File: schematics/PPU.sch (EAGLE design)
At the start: 51 parts, among them Q1 KN2222A, Q2 KIA431, Q3 2SC945, U12 UM6618, U13 53.693175MHz, U3 UM70C188, U4 KA2195D, U5 UM611024, U6 UM611024

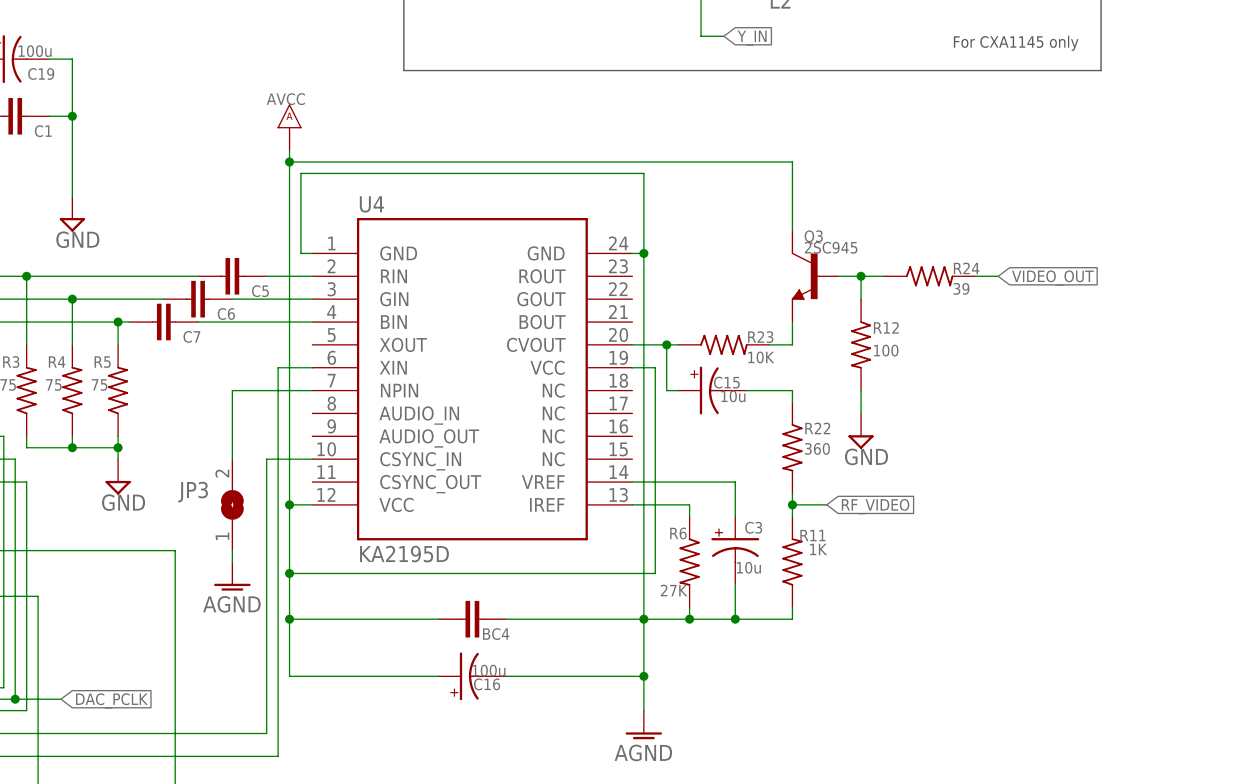
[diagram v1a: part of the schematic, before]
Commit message: Correct Q3 related wiring
(CV output)
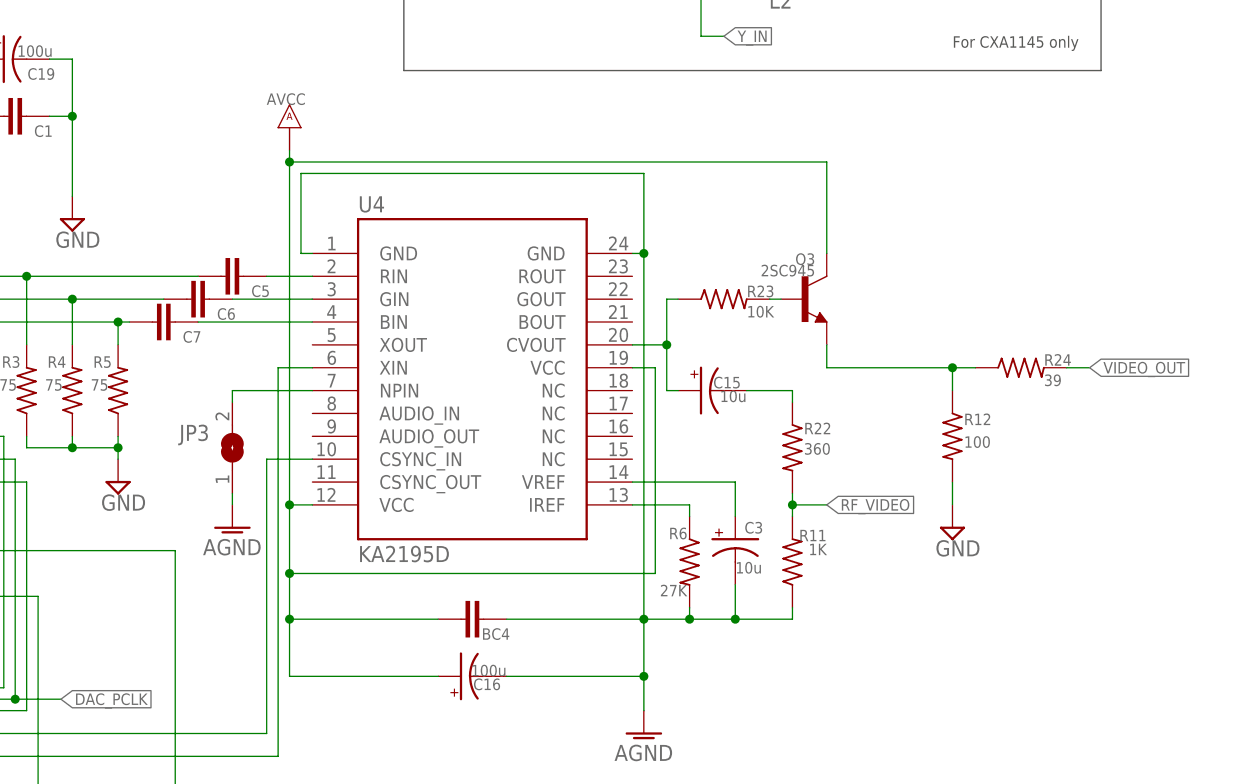
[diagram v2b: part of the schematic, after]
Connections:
- removed net N$28: Q3.B, R12.1, R24.1
- new net N$43: Q3.E, R12.1, R24.1
- net N$12: now also Q3.B; no longer Q3.E
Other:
- moved on the sheet: JP3, Q3, R12, R23, R24
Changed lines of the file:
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@@
 <?xml version="1.0" encoding="utf-8"?>
 <!DOCTYPE eagle SYSTEM "eagle.dtd">
-<eagle version="9.6.1">
+<eagle version="9.6.2">
 <drawing>
 <settings>
@@
 <attribute name="VALUE" x="212.725" y="169.545" size="1.778" layer="96"/>
 </instance>
-<instance part="AGND1" gate="VR1" x="222.25" y="80.01" smashed="yes">
-<attribute name="VALUE" x="222.25" y="78.74" size="1.778" layer="96" align="top-center"/>
+<instance part="AGND1" gate="VR1" x="222.25" y="86.36" smashed="yes">
+<attribute name="VALUE" x="222.25" y="85.09" size="1.778" layer="96" align="top-center"/>
 </instance>
 <instance part="JP1" gate="G$1" x="68.58" y="58.42" smashed="yes">
@@
 <attribute name="VALUE" x="279.4" y="101.6" size="1.27" layer="96" rot="MR0" align="top-left"/>
 </instance>
-<instance part="R23" gate="G$1" x="276.86" y="106.68" smashed="yes">
-<attribute name="NAME" x="279.4" y="106.9086" size="1.27" layer="95"/>
-<attribute name="VALUE" x="279.4" y="105.918" size="1.27" layer="96" align="top-left"/>
+<instance part="R23" gate="G$1" x="276.86" y="111.76" smashed="yes">
+<attribute name="NAME" x="279.4" y="111.9886" size="1.27" layer="95"/>
+<attribute name="VALUE" x="279.4" y="110.998" size="1.27" layer="96" align="top-left"/>
 </instance>
 <instance part="R22" gate="G$1" x="284.48" y="95.25" smashed="yes" rot="R270">
@@
 <attribute name="VALUE" x="288.29" y="83.312" size="1.27" layer="96" rot="R180" align="top-left"/>
 </instance>
-<instance part="Q3" gate="G$1" x="287.02" y="114.3" smashed="yes" rot="MR0">
-<attribute name="NAME" x="285.75" y="118.11" size="1.27" layer="95"/>
-<attribute name="VALUE" x="285.75" y="116.84" size="1.27" layer="96"/>
-</instance>
-<instance part="R24" gate="G$1" x="299.72" y="114.3" smashed="yes">
-<attribute name="NAME" x="302.26" y="114.5286" size="1.27" layer="95"/>
-<attribute name="VALUE" x="302.26" y="113.538" size="1.27" layer="96" align="top-left"/>
-</instance>
-<instance part="R12" gate="G$1" x="292.1" y="106.68" smashed="yes" rot="R270">
-<attribute name="NAME" x="293.37" y="107.9246" size="1.27" layer="95"/>
-<attribute name="VALUE" x="293.37" y="106.68" size="1.27" layer="96" align="top-left"/>
-</instance>
-<instance part="SUPPLY12" gate="GND" x="292.1" y="96.52" smashed="yes">
-<attribute name="VALUE" x="290.195" y="93.345" size="1.778" layer="96"/>
+<instance part="Q3" gate="G$1" x="285.75" y="111.76" smashed="yes">
+<attribute name="NAME" x="287.02" y="115.57" size="1.27" layer="95" rot="MR0"/>
+<attribute name="VALUE" x="287.02" y="114.3" size="1.27" layer="96" rot="MR0"/>
+</instance>
+<instance part="R24" gate="G$1" x="309.88" y="104.14" smashed="yes">
+<attribute name="NAME" x="312.42" y="104.3686" size="1.27" layer="95"/>
+<attribute name="VALUE" x="312.42" y="103.378" size="1.27" layer="96" align="top-left"/>
+</instance>
+<instance part="R12" gate="G$1" x="302.26" y="96.52" smashed="yes" rot="R270">
+<attribute name="NAME" x="303.53" y="97.7646" size="1.27" layer="95"/>
+<attribute name="VALUE" x="303.53" y="96.52" size="1.27" layer="96" align="top-left"/>
+</instance>
+<instance part="SUPPLY12" gate="GND" x="302.26" y="86.36" smashed="yes">
+<attribute name="VALUE" x="300.355" y="83.185" size="1.778" layer="96"/>
 </instance>
 <instance part="Q2" gate="G$1" x="228.6" y="48.26" smashed="yes" rot="R180">
@@
 <attribute name="VALUE" x="207.645" y="88.265" size="1.778" layer="96"/>
 </instance>
-<instance part="JP3" gate="1" x="222.25" y="88.9" smashed="yes" rot="R90">
-<attribute name="NAME" x="219.71" y="91.44" size="1.778" layer="95" rot="R180"/>
-<attribute name="VALUE" x="226.06" y="86.36" size="1.778" layer="96" rot="R90"/>
+<instance part="JP3" gate="1" x="222.25" y="95.25" smashed="yes" rot="R90">
+<attribute name="NAME" x="219.71" y="97.79" size="1.778" layer="95" rot="R180"/>
+<attribute name="VALUE" x="226.06" y="92.71" size="1.778" layer="96" rot="R90"/>
 </instance>
 </instances>
@@
 <pinref part="JP3" gate="1" pin="1"/>
 <pinref part="AGND1" gate="VR1" pin="AGND"/>
-<wire x1="222.25" y1="83.82" x2="222.25" y2="82.55" width="0.1524" layer="91"/>
+<wire x1="222.25" y1="90.17" x2="222.25" y2="88.9" width="0.1524" layer="91"/>
 </segment>
 </net>
@@
 <segment>
 <pinref part="R12" gate="G$1" pin="2"/>
-<wire x1="292.1" y1="101.6" x2="292.1" y2="99.06" width="0.1524" layer="91"/>
+<wire x1="302.26" y1="91.44" x2="302.26" y2="88.9" width="0.1524" layer="91"/>
 <pinref part="SUPPLY12" gate="GND" pin="GND"/>
 </segment>
@@
 <wire x1="222.25" y1="101.6" x2="231.14" y2="101.6" width="0.1524" layer="91"/>
 <pinref part="JP3" gate="1" pin="2"/>
-<wire x1="222.25" y1="93.98" x2="222.25" y2="101.6" width="0.1524" layer="91"/>
+<wire x1="222.25" y1="100.33" x2="222.25" y2="101.6" width="0.1524" layer="91"/>
 </segment>
 </net>
@@
 <pinref part="C16" gate="G$1" pin="+"/>
 <wire x1="228.6" y1="69.85" x2="245.11" y2="69.85" width="0.1524" layer="91"/>
+<wire x1="288.29" y1="127" x2="228.6" y2="127" width="0.1524" layer="91"/>
+<junction x="228.6" y="127"/>
 <pinref part="Q3" gate="G$1" pin="C"/>
-<wire x1="284.48" y1="119.38" x2="284.48" y2="127" width="0.1524" layer="91"/>
-<wire x1="284.48" y1="127" x2="228.6" y2="127" width="0.1524" layer="91"/>
-<junction x="228.6" y="127"/>
+<wire x1="288.29" y1="116.84" x2="288.29" y2="127" width="0.1524" layer="91"/>
 </segment>
 </net>
@@
 <segment>
 <pinref part="U4" gate="G$1" pin="CVOUT"/>
-<pinref part="R23" gate="G$1" pin="1"/>
-<wire x1="271.78" y1="106.68" x2="270.51" y2="106.68" width="0.1524" layer="91"/>
 <pinref part="C15" gate="G$1" pin="+"/>
 <wire x1="270.51" y1="106.68" x2="266.7" y2="106.68" width="0.1524" layer="91"/>
 <wire x1="271.78" y1="101.6" x2="270.51" y2="101.6" width="0.1524" layer="91"/>
 <wire x1="270.51" y1="101.6" x2="270.51" y2="106.68" width="0.1524" layer="91"/>
+<wire x1="270.51" y1="106.68" x2="270.51" y2="111.76" width="0.1524" layer="91"/>
 <junction x="270.51" y="106.68"/>
+<pinref part="R23" gate="G$1" pin="1"/>
+<wire x1="270.51" y1="111.76" x2="271.78" y2="111.76" width="0.1524" layer="91"/>
 </segment>
 </net>
@@
 </segment>
 </net>
-<net name="N$28" class="0">
-<segment>
-<pinref part="Q3" gate="G$1" pin="B"/>
-<pinref part="R24" gate="G$1" pin="1"/>
-<wire x1="289.56" y1="114.3" x2="292.1" y2="114.3" width="0.1524" layer="91"/>
-<pinref part="R12" gate="G$1" pin="1"/>
-<wire x1="292.1" y1="114.3" x2="294.64" y2="114.3" width="0.1524" layer="91"/>
-<wire x1="292.1" y1="111.76" x2="292.1" y2="114.3" width="0.1524" layer="91"/>
-<junction x="292.1" y="114.3"/>
-</segment>
-</net>
 <net name="VIDEO_OUT" class="0">
 <segment>
 <pinref part="R24" gate="G$1" pin="2"/>
-<wire x1="304.8" y1="114.3" x2="307.34" y2="114.3" width="0.1524" layer="91"/>
-<label x="307.34" y="114.3" size="1.27" layer="95" xref="yes"/>
+<wire x1="314.96" y1="104.14" x2="317.5" y2="104.14" width="0.1524" layer="91"/>
+<label x="317.5" y="104.14" size="1.27" layer="95" xref="yes"/>
 </segment>
 </net>
@@
 <wire x1="76.2" y1="63.5" x2="73.66" y2="63.5" width="0.1524" layer="91"/>
 <label x="73.66" y="63.5" size="1.27" layer="95" rot="MR0" xref="yes"/>
-</segment>
-</net>
-<net name="N$12" class="0">
-<segment>
-<pinref part="R23" gate="G$1" pin="2"/>
-<wire x1="281.94" y1="106.68" x2="284.48" y2="106.68" width="0.1524" layer="91"/>
-<pinref part="Q3" gate="G$1" pin="E"/>
-<wire x1="284.48" y1="106.68" x2="284.48" y2="109.22" width="0.1524" layer="91"/>
 </segment>
 </net>
@@
 </segment>
 </net>
+<net name="N$12" class="0">
+<segment>
+<pinref part="R23" gate="G$1" pin="2"/>
+<pinref part="Q3" gate="G$1" pin="B"/>
+<wire x1="281.94" y1="111.76" x2="283.21" y2="111.76" width="0.1524" layer="91"/>
+</segment>
+</net>
+<net name="N$43" class="0">
+<segment>
+<pinref part="Q3" gate="G$1" pin="E"/>
+<wire x1="288.29" y1="106.68" x2="288.29" y2="104.14" width="0.1524" layer="91"/>
+<wire x1="288.29" y1="104.14" x2="302.26" y2="104.14" width="0.1524" layer="91"/>
+<pinref part="R24" gate="G$1" pin="1"/>
+<pinref part="R12" gate="G$1" pin="1"/>
+<wire x1="302.26" y1="104.14" x2="304.8" y2="104.14" width="0.1524" layer="91"/>
+<wire x1="302.26" y1="101.6" x2="302.26" y2="104.14" width="0.1524" layer="91"/>
+<junction x="302.26" y="104.14"/>
+</segment>
+</net>
